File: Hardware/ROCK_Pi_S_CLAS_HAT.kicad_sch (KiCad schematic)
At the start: 13 parts, among them J1 ROCK_Pi_S, J2 DX07S016JA1R1500, U1 BPI-9600, U2 USBLC6-2SC6, U3 MIC5219-3.3YM5

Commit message: フットプリントの割り当てまで完了
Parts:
- added BT1: MS421R, Battery_extlib:Battery_Seiko_MS421R, symbol Device:Battery_Cell
- added C10, C11, C12, C9: 1u, Capacitor_SMD:C_0603_1608Metric, symbol Device:C_Small
- added C5: GJM1555C1H470FB01D, Capacitor_SMD_extlib:C_Murata_xxx15_0402_1005Metric_1.0x0.5mm, symbol Device:C_Small
- added C6, C7: 0.1u, Capacitor_SMD:C_0603_1608Metric, symbol Device:C_Small
- added C8: 2.2u, Capacitor_SMD:C_0603_1608Metric, symbol Device:C_Small
- added D3: AXGD10402KR, Diode_SMD_extlib:D_Littelfuse_AXGD10402KR_0402_1005Metric_1.02x0.51mm, symbol Device:D_TVS_Small
- added D4, D5: CUHS20S30, Diode_SMD_extlib:D_Toshiba_US2H, symbol Device:D_Schottky_Small
- added D6: PULSE, LED_SMD:LED_0603_1608Metric, symbol Device:LED_Small
- added D7: RTK, LED_SMD:LED_0603_1608Metric, symbol Device:LED_Small
- added J3: U.FL-R-SMT-1, Connector_Coaxial:U.FL_Hirose_U.FL-R-SMT-1_Vertical, symbol Connector:Conn_Coaxial
- added J4: DX07S016JA1R1500, Connector_USB:USB_C_Receptacle_JAE_DX07S016JA1R1500, symbol Connector:USB_C_Receptacle_USB2.0_14P
- added L1: LQW18ANR12G80D, Inductor_SMD_extlib:L_Murata_LQW18ANxxxx80x_0603_1608Metric_1.65x0.99mm, symbol Device:L_Small
- added Q1, Q2: AO3400A, Package_TO_SOT_SMD:SOT-23, symbol Transistor_FET:AO3400A
- added R10, R11, R14, R15, R9: 33, Resistor_SMD:R_0603_1608Metric, symbol Device:R_Small
- added R12, R13, R7, R8: 27, Resistor_SMD:R_0603_1608Metric, symbol Device:R_Small
- added R16, R17: 1k, Resistor_SMD:R_0603_1608Metric, symbol Device:R_Small
- added R18: 3.3k, Resistor_SMD:R_0603_1608Metric, symbol Device:R_Small
- added R19, R24: 100k, Resistor_SMD:R_0603_1608Metric, symbol Device:R_Small
- added R20, R23: 10k, Resistor_SMD:R_0603_1608Metric, symbol Device:R_Small
- added R21, R22: 47, Resistor_SMD:R_0603_1608Metric, symbol Device:R_Small
- added R3: 10, Resistor_SMD:R_0603_1608Metric, symbol Device:R_Small
- added R4: 100, Resistor_SMD_extlib:R_Vishay_FC0603xxxxxxTxx_0603_1608Metric_1.626x0.813mm, symbol Device:R_Small
- added R5, R6: 5.1k, Resistor_SMD:R_0603_1608Metric, symbol Device:R_Small
- added TP1: EXTINT_F9R, TestPoint:TestPoint_Pad_D1.0mm, symbol Connector:TestPoint_Small
- added TP2: ~{SAFEBOOT_F9R}, TestPoint:TestPoint_Pad_D1.0mm, symbol Connector:TestPoint_Small
- added TP3: ~{RESET_F9R}, TestPoint:TestPoint_Pad_D1.0mm, symbol Connector:TestPoint_Small
- added TP4: EXTINT_D9C, TestPoint:TestPoint_Pad_D1.0mm, symbol Connector:TestPoint_Small
- added TP5: ~{SAFEBOOT_D9C}, TestPoint:TestPoint_Pad_D1.0mm, symbol Connector:TestPoint_Small
- added TP6: ~{RESET_D9C}, TestPoint:TestPoint_Pad_D1.0mm, symbol Connector:TestPoint_Small
- added U4: ZED-F9R, RF_GPS:ublox_ZED, symbol RF_GPS:ZED-F9P
- added U5: NEO-D9C, RF_GNSS_extlib:ublox_NEO, symbol RF_GNSS_extlib:NEO-D9C
- added U6: PD0922J5050S2HF, RF_Converter_extlib:Xinger_0805_2012Metric-6_Pad0.33x0.41mm, symbol RF_Converter_extlib:PD0922J5050S2HF
- added U7: USBLC6-2SC6, Package_TO_SOT_SMD:SOT-23-6, symbol Power_Protection:USBLC6-2SC6
- C1, C2, C4: footprint (none) -> Capacitor_SMD:C_0603_1608Metric
- C3: footprint (none) -> Capacitor_SMD:C_0805_2012Metric
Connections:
- net +3.3V: now also C10.1, C9.1, D5.2 (A), Q1.3 (D), Q2.3 (D), R17.1, U4.33 (VCC), U4.34 (VCC), U5.23 (VCC)
- net GND: now also BT1.2 (-), C10.2, C11.2, C12.2, C6.2, C7.2, C8.2, C9.2, D3.1 (A1), D6.1 (K), J3.2 (Ext), J4.A1 (GND), J4.A12 (GND), J4.B1 (GND), J4.B12 (GND), J4.S1 (SHIELD), R19.2, R20.2, R23.2, R24.2, R5.2, R6.2, U4.1 (GND), U4.12 (GND), U4.14 (GND), U4.3 (GND), U4.32 (GND), U4.37 (GND), U4.41 (GND), U4.48 (GND), U4.55 (GND), U5.10 (GND), U5.12 (GND), U5.13 (GND), U5.24 (GND), U6.1 (GND), U6.3 (GND), U6.5 (GND), U7.2 (GND)
- net VDD: now reaches C4.1, D1.1 (K), D2.1 (K), U3.1 (IN), U3.3 (EN)
- net VDD: now also D4.1 (K)
- net RXD0_ROCK: now reaches J1.10 (Pin_10)
- net TP: now reaches J1.11 (Pin_11)
- net TP: now also R16.1, U4.53 (TIMEPULSE)
- net RTK: now reaches J1.13 (Pin_13)
- net RTK: now also D7.1 (K), U4.20 (RTK_STAT)
- net GEO: now reaches J1.15 (Pin_15)
- net GEO: now also U4.19 (GEOFENCE_STAT)
- net RXD2_ROCK: now reaches J1.21 (Pin_21)
- net RXD2_ROCK: now also R10.2
- net RXD1_ROCK: now reaches J1.23 (Pin_23)
- net RXD1_ROCK: now also R9.2
- net TXD1_ROCK: now reaches J1.24 (Pin_24)
- net TXD1_ROCK: now also U4.43 (RXD/SPI_MOSI)
- net SDA1: now reaches J1.3 (Pin_3)
- net SDA1: now also R11.2, R15.1
- net SCL1: now reaches J1.5 (Pin_5)
- net SCL1: now also U4.45 (SCL/SPI_CLK), U5.19 (SCL/SPI_CLK)
- net TX_READY_F9R: now reaches J1.7 (Pin_7)
- net TX_READY_F9R: now also U4.46 (TX_READY)
- net TXD0_ROCK: now reaches J1.8 (Pin_8)
- net D+ renamed D+F9R
- net D+F9R: now also R8.2
- net D- renamed D-F9R
- net D-F9R: now also R7.2
- net VBUS renamed VBUS_F9R
- net VBUS_F9R: now also R21.1
- new net: C5.1, D3.2 (A2), J3.1 (In), L1.2
- new net: R13.2, U5.6 (USB_DP)
- new net: R10.1, U4.27 (TXD2)
- new net: R7.1, U4.39 (USB_DM)
- new net: C6.1, L1.1, R3.2
- new net: R11.1, U4.44 (SDA/~{SPI_CS})
- new net: Q2.1 (G), R22.2, R23.1
- new net: TP3.1, U4.49 (~{RESET})
- new net: R12.2, U5.5 (USB_DM)
- new net: D5.1 (K), R18.1
- new net: Q1.1 (G), R20.1, R21.2
- new net: R8.1, U4.40 (USB_DP)
- new net: TP5.1, U5.1 (~{SAFEBOOT})
- new net: TP4.1, U5.17 (EXTINT)
- new net: R15.2, U5.18 (SDA/~{SPI_CS})
- new net: R14.2, U5.20 (TXD/SPI_MISO)
- new net: TP6.1, U5.8 (~{RESET})
- new net: TP2.1, U4.50 (~{SAFEBOOT})
- new net: J4.A5 (CC1), R5.1
- new net: J4.A6 (D+), J4.B6 (D+), U7.3 (I/O2)
- new net: J4.A7 (D-), J4.B7 (D-), U7.1 (I/O1)
- new net: J4.B5 (CC2), R6.1
- new net: R14.1, U4.26 (RXD2)
- new net: R9.1, U4.42 (TXD/SPI_MISO)
- new net: TP1.1, U4.51 (EXTINT)
- new net: C5.2, U6.2 (Input)
- new net: D6.2 (A), R16.2
- new net: D7.2 (A), R17.2
- new net +3.3VA: R3.1, U4.7 (VCC_RF)
- new net +BATT: BT1.1 (+), C8.1, R18.2, U4.36 (V_BCKP)
- new net D+D9C: R13.1, U7.4 (I/O2)
- new net D-D9C: R12.1, U7.6 (I/O1)
- new net RF_IN_D9C: R4.2, U5.11 (RF_IN), U6.6 (Output2)
- new net RF_IN_F9R: R4.1, U4.2 (RF_IN), U6.4 (Output1)
- new net VBUS_D9C: C7.1, D4.2 (A), J4.A4 (VBUS), J4.A9 (VBUS), J4.B4 (VBUS), J4.B9 (VBUS), R22.1, U7.5 (VBUS)
- new net V_USB_D9C: C12.1, Q2.2 (S), R24.1, U5.7 (V_USB)
- new net V_USB_F9R: C11.1, Q1.2 (S), R19.1, U4.38 (V_USB)
- no-connect marks 27 -> 42
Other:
- note added: "->"
- note added: "<-"
- note added: "DC-Blocking"
- note added: "I2C+UART only"
- note added: "Interface"
- note added: "Power"
- note added: "RF"
- note added: "USB availability detection"
- moved on the sheet: C1, C2, C3, C4, D1, D2, J1A, J1B, J1C, J2, R1, R2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

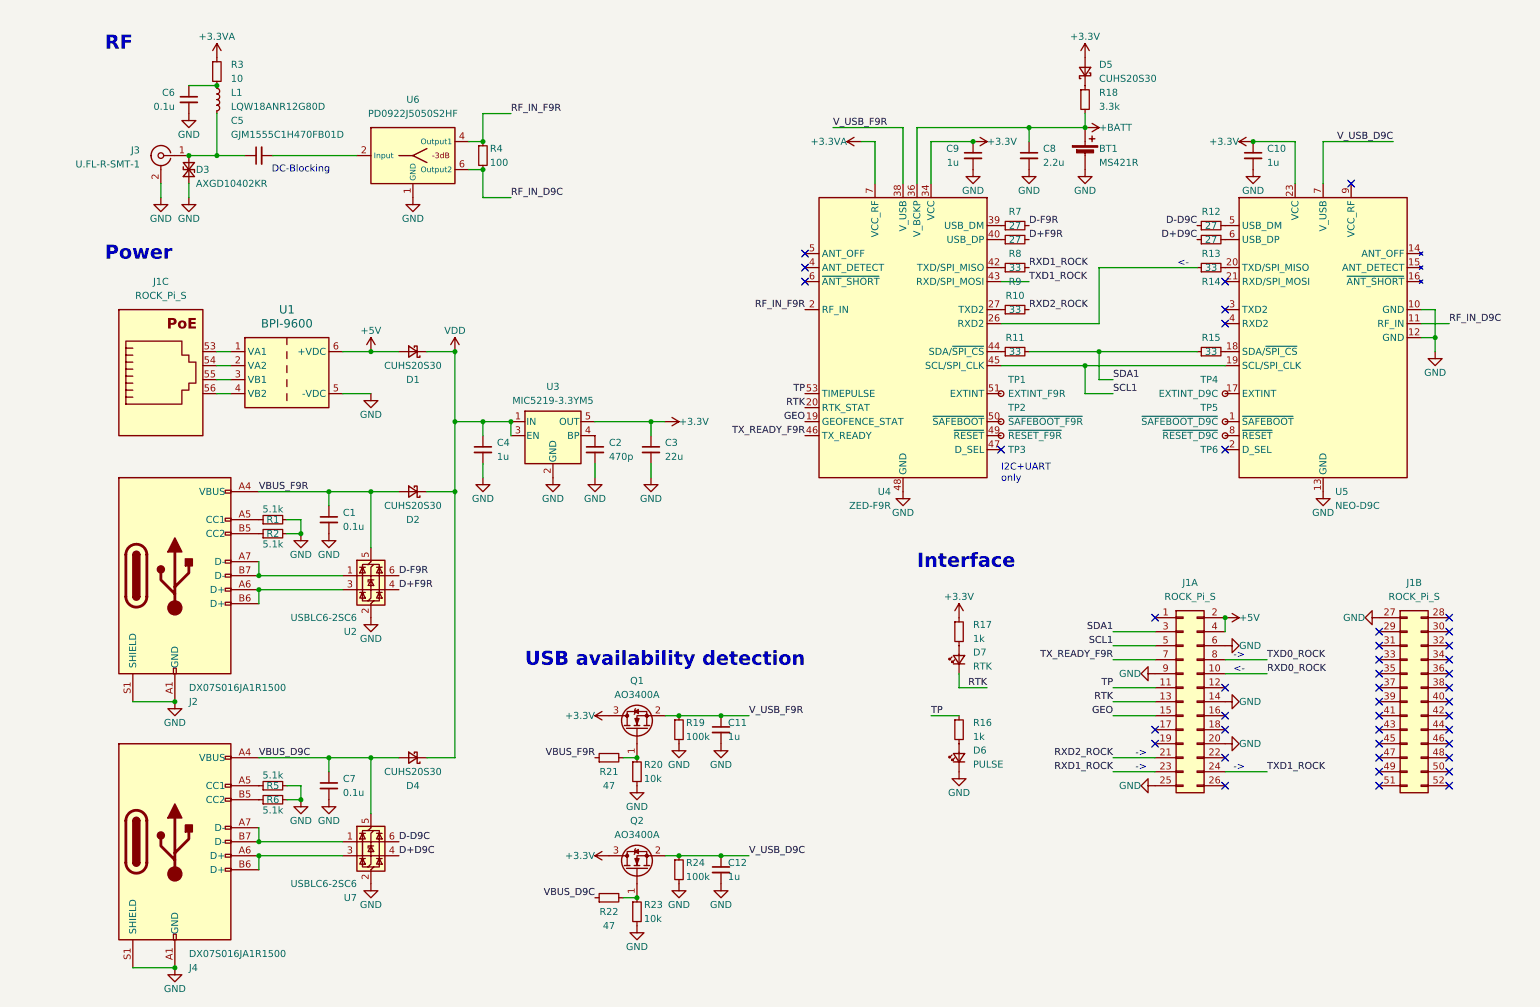
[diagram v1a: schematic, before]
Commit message: LCSC番号を割り当て
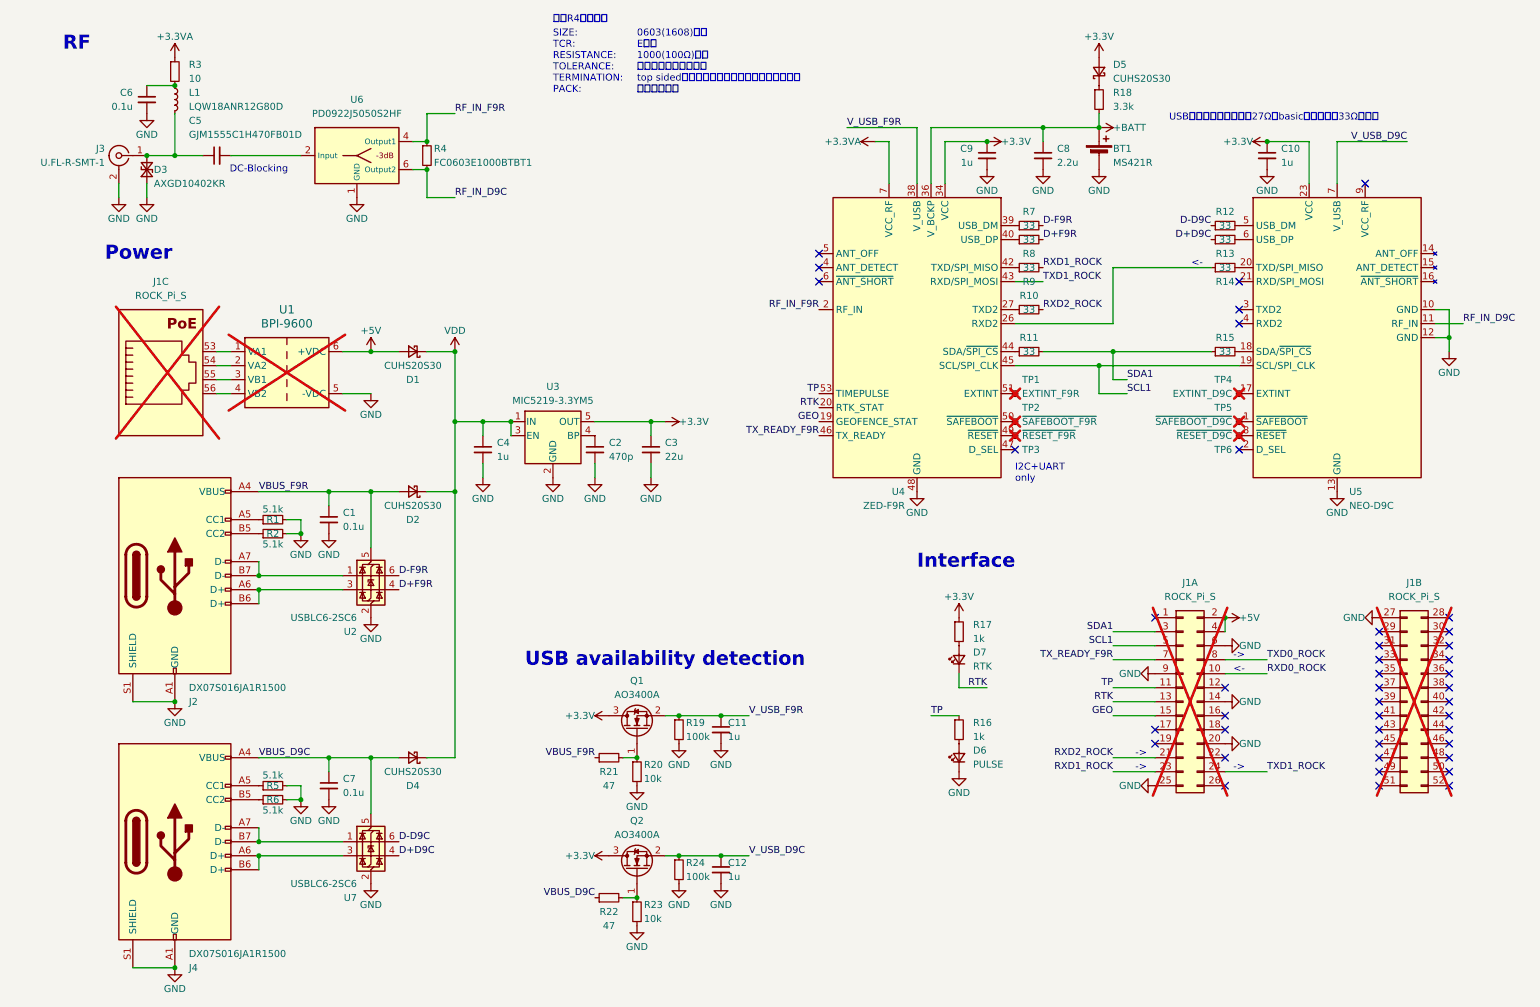
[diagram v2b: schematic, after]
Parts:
- BT1: Remark (none) -> No stock
- C1, C6, C7: LCSC (none) -> C14663; Remark (none) -> basic
- C10, C11, C12, C4, C9: LCSC (none) -> C15849; Remark (none) -> basic
- C2: LCSC (none) -> C1620; Remark (none) -> basic
- C3: LCSC (none) -> C45783; Remark (none) -> basic
- C5: LCSC (none) -> C882562
- C8: LCSC (none) -> C23630; Remark (none) -> basic
- D1, D2, D4, D5: LCSC (none) -> C5636538
- D3: LCSC (none) -> C434715
- D6: LCSC (none) -> C2290; Remark (none) -> basic
- D7: LCSC (none) -> C2286; Remark (none) -> basic
- J1, TP1, TP2, TP3, TP4, TP5, TP6, U1: now not fitted
- J2, J4: LCSC (none) -> C3197885; Remark (none) -> Low Stock
- J3: LCSC (none) -> C88374
- L1: LCSC (none) -> C307612
- Q1, Q2: LCSC (none) -> C20917; Remark (none) -> basic
- R1, R2, R5, R6: LCSC (none) -> C23186; Remark (none) -> basic
- R10, R11, R14, R15, R9: LCSC (none) -> C23140; Remark (none) -> basic
- R12, R13, R7, R8: value 27 -> 33; LCSC (none) -> C23140; Remark (none) -> basic
- R16, R17: LCSC (none) -> C21190; Remark (none) -> basic
- R18: LCSC (none) -> C22978; Remark (none) -> basic
- R19, R24: LCSC (none) -> C25803; Remark (none) -> basic
- R20, R23: LCSC (none) -> C25804; Remark (none) -> basic
- R21, R22: LCSC (none) -> C23182; Remark (none) -> basic
- R3: LCSC (none) -> C22859; Remark (none) -> basic
- R4: value 100 -> FC0603E1000BTBT1; LCSC (none) -> C3999268; Remark (none) -> Out of Stock
- U2, U7: LCSC (none) -> C7519
- U3: LCSC (none) -> C29613
- U4: LCSC (none) -> C5189233; Remark (none) -> Out of Stock
- U5: LCSC (none) -> C5137014; Remark (none) -> Out of Stock
- U6: LCSC (none) -> C5136968; Remark (none) -> Out of Stock
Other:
- note added: "0603(1608)のみ Eのみ 1000(100Ω)のみ 高精度の方が望ましい top sidedのうち鉛フリーでないものが望ましい どれでもよい"
- note added: "SIZE: TCR: RESISTANCE: TOLERANCE: TERMINATION: PACK:"
- note added: "USBのダンピング抵抗の27Ωはbasicに無いため33Ωに統一"
- note added: "抵抗R4について"
- moved on the sheet: BT1, C10, C5, C6, C8, C9, D3, D5, J3, L1, R10, R11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

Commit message: LED追加
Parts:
- added D8: PWR(RED), LED_SMD:LED_0603_1608Metric, symbol Device:LED_Small
- added R25: 1k, Resistor_SMD:R_0603_1608Metric, symbol Device:R_Small
- D6: value PULSE -> PULSE(WHITE)
- D7: value RTK -> RTK(YELLOW); LCSC C2286 -> C72038
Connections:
- net +3.3V: now also R25.1
- net GND: now also D8.1 (K)
- new net: D8.2 (A), R25.2

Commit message: USBコネクタを変更
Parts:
- C5, D1, D2, D3, D4, D5, J3, L1, U2, U3, U7: Remark (none) -> Extended
- C6: footprint Capacitor_SMD:C_0603_1608Metric -> Capacitor_SMD:C_0402_1005Metric; LCSC C14663 -> C307331
- J2, J4: value DX07S016JA1R1500 -> GT-USB-7025; footprint Connector_USB:USB_C_Receptacle_JAE_DX07S016JA1R1500 -> Connector_USB:USB_C_Receptacle_G-Switch_GT-USB-7025; LCSC C3197885 -> C963213; Remark Low Stock -> Extended
- R3: footprint Resistor_SMD:R_0603_1608Metric -> Resistor_SMD:R_0402_1005Metric; LCSC C22859 -> C25077
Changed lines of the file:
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@@
 			)
 		)
-		(property "Remark" ""
+		(property "Remark" "Extended"
 			(at 35.56 43.18 0)
 			(effects
@@
 			)
 		)
-		(property "Remark" ""
+		(property "Remark" "Extended"
 			(at 76.2 116.84 0)
 			(effects
@@
 			)
 		)
-		(property "Footprint" "Resistor_SMD:R_0603_1608Metric"
+		(property "Footprint" "Resistor_SMD:R_0402_1005Metric"
 			(at 40.64 25.4 0)
 			(effects
@@
 			)
 		)
-		(property "LCSC" "C22859"
+		(property "LCSC" "C25077"
 			(at 40.64 25.4 0)
 			(effects
@@
 			)
 		)
-		(property "Remark" ""
+		(property "Remark" "Extended"
 			(at 83.82 149.86 0)
 			(effects
@@
 			)
 		)
-		(property "Remark" ""
+		(property "Remark" "Extended"
 			(at 40.64 30.48 0)
 			(effects
@@
 			)
 		)
-		(property "Remark" ""
+		(property "Remark" "Extended"
 			(at 208.28 25.4 0)
 			(effects
@@
 			)
 		)
-		(property "Footprint" "Capacitor_SMD:C_0603_1608Metric"
+		(property "Footprint" "Capacitor_SMD:C_0402_1005Metric"
 			(at 35.56 30.48 0)
 			(effects
@@
 			)
 		)
-		(property "LCSC" "C14663"
+		(property "LCSC" "C307331"
 			(at 35.56 30.48 0)
 			(effects
@@
 			)
 		)
-		(property "Value" "DX07S016JA1R1500"
+		(property "Value" "GT-USB-7025"
 			(at 43.18 137.16 0)
 			(effects
@@
 			)
 		)
-		(property "Footprint" "Connector_USB:USB_C_Receptacle_JAE_DX07S016JA1R1500"
+		(property "Footprint" "Connector_USB:USB_C_Receptacle_G-Switch_GT-USB-7025"
 			(at 44.45 116.84 0)
 			(effects
@@
 			)
 		)
-		(property "LCSC" "C3197885"
+		(property "LCSC" "C963213"
 			(at 40.64 116.84 0)
 			(effects
@@
 			)
 		)
-		(property "Remark" "Low Stock"
+		(property "Remark" "Extended"
 			(at 40.64 116.84 0)
 			(effects
@@
 			)
 		)
-		(property "Value" "DX07S016JA1R1500"
+		(property "Value" "GT-USB-7025"
 			(at 43.18 185.42 0)
 			(effects
@@
 			)
 		)
-		(property "Footprint" "Connector_USB:USB_C_Receptacle_JAE_DX07S016JA1R1500"
+		(property "Footprint" "Connector_USB:USB_C_Receptacle_G-Switch_GT-USB-7025"
 			(at 44.45 165.1 0)
 			(effects
@@
 			)
 		)
-		(property "LCSC" "C3197885"
+		(property "LCSC" "C963213"
 			(at 40.64 165.1 0)
 			(effects
@@
 			)
 		)
-		(property "Remark" "Low Stock"
+		(property "Remark" "Extended"
 			(at 40.64 165.1 0)
 			(effects
@@
 			)
 		)
-		(property "Remark" ""
+		(property "Remark" "Extended"
 			(at 30.48 40.64 0)
 			(effects
@@
 			)
 		)
-		(property "Remark" ""
+		(property "Remark" "Extended"
 			(at 48.26 40.64 0)
 			(effects
@@
 			)
 		)
-		(property "Remark" ""
+		(property "Remark" "Extended"
 			(at 83.82 101.6 0)
 			(effects
@@
 			)
 		)
-		(property "Remark" ""
+		(property "Remark" "Extended"
 			(at 83.82 76.2 0)
 			(effects
@@
 			)
 		)
-		(property "Remark" ""
+		(property "Remark" "Extended"
 			(at 76.2 165.1 0)
 			(effects
@@
 			)
 		)
-		(property "Remark" ""
+		(property "Remark" "Extended"
 			(at 109.22 91.44 0)
 			(effects
